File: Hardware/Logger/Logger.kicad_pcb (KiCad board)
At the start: 2 copper layers, 70 x 71 mm, 78 parts, among them CN1 Conn_02x19_Odd_Even, CN10 Conn_02x19_Odd_Even, CN2 Conn_02x19_Odd_Even, CN7 Conn_02x19_Odd_Even, J1 Conn_Coaxial, J10 Conn_01x08_Female, J2 Conn_Coaxial, J3 Conn_Coaxial, J4 Conn_Coaxial, J5 USB_B_Micro, J6 112K-TAA0-RA1_ATTEND, J7 DB9_Female_MountingHoles, J8 Conn_01x06_Female, J9 Conn_01x08_Female, Q5 BC848, Q6 BC848, Q7 BC848, Q8 BC848, SW1 SW_Push, SW2 SW_Push, SW3 SW_Push, SW4 SW_Push, U1 ESP-12E, U2 ST7735S, U3 LD1117ASTR

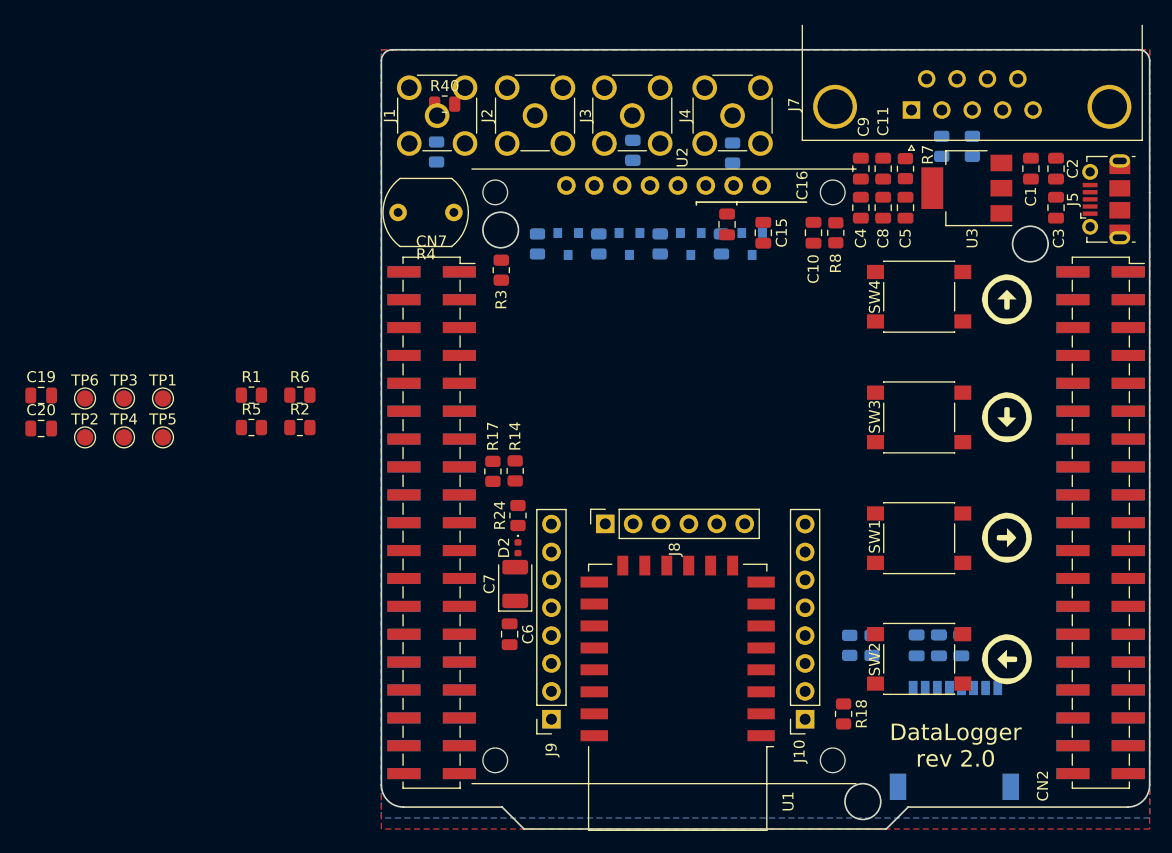
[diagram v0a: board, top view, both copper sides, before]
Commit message: draft of rev 3.0, cleanup of repo from not fully open source libs
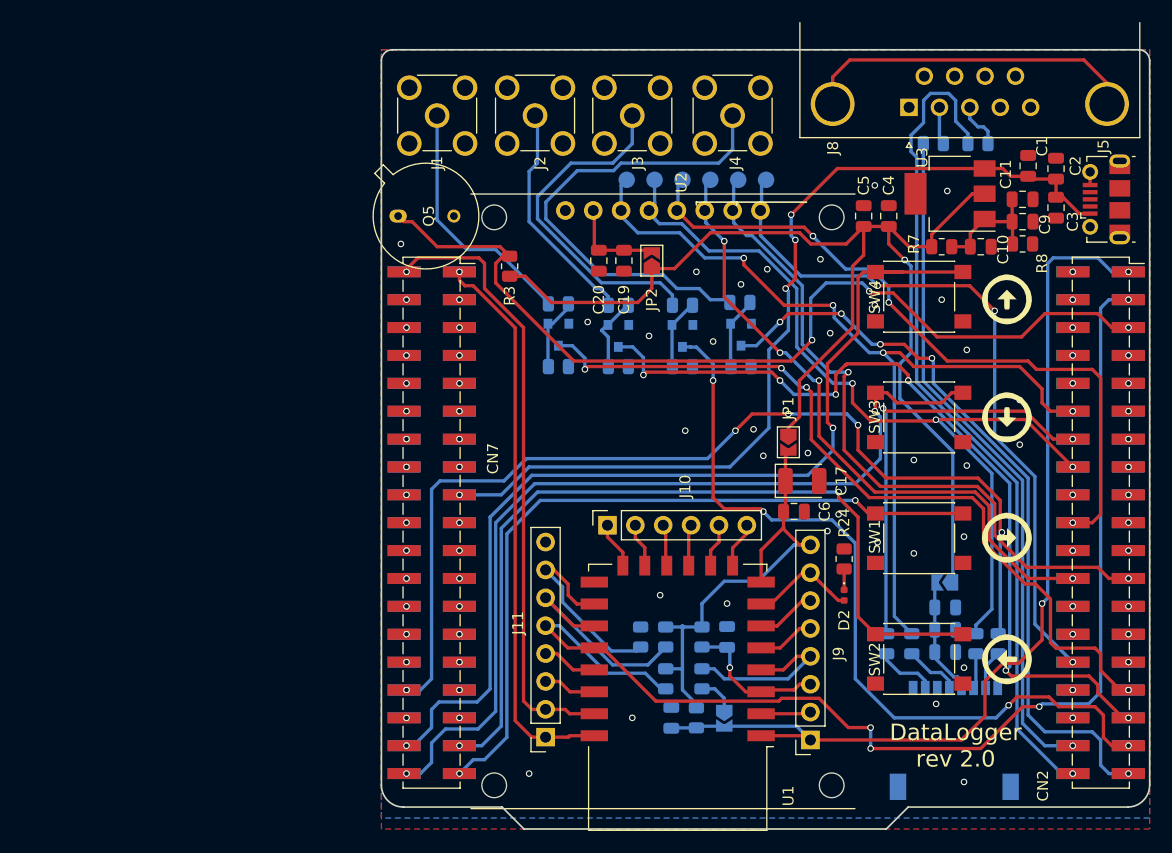
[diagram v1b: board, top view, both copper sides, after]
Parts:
- removed C7: 47u/6V3, Capacitor_Tantalum_SMD:CP_EIA-3528-21_Kemet-B
- removed C8: 330n, Capacitor_SMD:C_0805_2012Metric
- removed J7: DB9_Female_MountingHoles, Connector_Dsub:DSUB-9_Female_Horizontal_P2.77x2.84mm_EdgePinOffset4.94mm_Housed_MountingHolesOffset7.48mm
- removed R4: R_PHOTO, OptoDevice:R_LDR_7x6mm_P5.1mm_Vertical
- added C17: 47u/6V3, Capacitor_Tantalum_SMD:CP_EIA-3528-21_Kemet-B, F.Cu at (168.4, 90.3)
- added J11: Conn_01x08_Socket, Connector_PinSocket_2.54mm:PinSocket_1x08_P2.54mm_Vertical, F.Cu at (145.0, 113.6)
- added JP1: Jumper_2_Small_Open, Jumper:SolderJumper-2_P1.3mm_Open_TrianglePad1.0x1.5mm, F.Cu at (167.1, 86.8)
- added JP2: Jumper_2_Small_Open, Jumper:SolderJumper-2_P1.3mm_Open_TrianglePad1.0x1.5mm, F.Cu at (154.6, 70.2)
- added JP4: Jumper_2_Small_Open, Jumper:SolderJumper-2_P1.3mm_Open_TrianglePad1.0x1.5mm, B.Cu at (181.3, 99.5)
- added JP5: Jumper_2_Small_Open, Jumper:SolderJumper-2_P1.3mm_Open_TrianglePad1.0x1.5mm, B.Cu at (161.2, 111.9)
- added Q5: Q_Photo_NPN, Package_TO_SOT_THT:TO-5-2, F.Cu at (131.5, 66.2)
- added R15: 470R, Resistor_SMD:R_0805_2012Metric, B.Cu at (159.2, 108.3)
- C15, C16, R1, R14, R17, R18, R2, R40, R5, R6, TP1, TP2, TP3, TP4, TP5, TP6: moved to B.Cu
- J10: value Conn_01x08_Female -> Conn_01x06_Socket; footprint Connector_PinSocket_2.54mm:PinSocket_1x08_P2.54mm_Vertical -> Connector_PinSocket_2.54mm:PinSocket_1x06_P2.54mm_Vertical
- J8: value Conn_01x06_Female -> DE9_Plug_MountingHoles; footprint Connector_PinSocket_2.54mm:PinSocket_1x06_P2.54mm_Vertical -> Connector_Dsub:DSUB-9_Female_Horizontal_P2.77x2.84mm_EdgePinOffset4.94mm_Housed_MountingHolesOffset7.48mm
- J9: value Conn_01x08_Female -> Conn_01x08_Socket
- R3: value 1k -> 2M
- moved R1 71.7 mm to (186.2, 105.1), turned to -90 degrees
- moved TP2 66.3 mm to (165.1, 62.9), turned to 180 degrees
- moved R2 64.7 mm to (184.2, 105.1), turned to -90 degrees
- moved R5 63.3 mm to (178.3, 105.1), turned to -90 degrees
- moved TP3 59.4 mm to (162.5, 62.9), turned to 180 degrees
- moved TP4 58.4 mm to (160.0, 62.9), turned to 180 degrees
- moved R6 58.1 mm to (176.0, 105.1), turned to -90 degrees
- moved TP6 55.6 mm to (154.9, 62.9), turned to 180 degrees
- moved C19 54.5 mm to (152.1, 70.2), turned to -90 degrees
- moved C20 53.1 mm to (149.8, 70.2), turned to -90 degrees
- moved TP5 52.8 mm to (157.4, 62.9), turned to 180 degrees
- moved J8 47.0 mm to (178.1, 56.2), turned to 180 degrees
- moved TP1 46.7 mm to (152.4, 62.9), turned to 180 degrees
- moved C16 45.2 mm to (156.4, 111.9), turned to 90 degrees
- moved C15 37.0 mm to (161.5, 104.5), turned to 90 degrees
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- renumbered Q5 to Q1, Q6 to Q2, Q7 to Q3, Q8 to Q4
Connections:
- net CS_ESP renamed Net-(CN10-Pin_18)
- net ESP_ENABLE renamed Net-(CN10-Pin_22)
- net MISO renamed SPI1_MISO
- net MOSI renamed SPI1_MOSI
- C12 pad 1: 3V3 -> Net-(J6-VDD)
- C13 pad 1: 3V3 -> Net-(J6-VDD)
- C14 pad 1: 3V3 -> Net-(J6-VDD)
- C19 pad 1: 3V3 -> Net-(JP2-B)
- C20 pad 1: 3V3 -> Net-(JP2-B)
- C6 pad 1: 3V3 -> ESP_PWR
- CN1 pad 1: Net-(CN1-Pad1) -> ESP32_RX
- CN1 pad 2: Net-(CN1-Pad2) -> ESP32_TX
- CN1 pad 31: Net-(CN1-Pad31) -> CS_SD
- CN1 pad 35: Net-(CN1-Pad35) -> KEY_RIGHT
- CN1 pad 36: Net-(CN1-Pad36) -> KEY_UP
- CN1 pad 37: Net-(CN1-Pad37) -> KEY_LEFT
- CN1 pad 38: Net-(CN1-Pad38) -> KEY_DOWN
- CN10 pad 10: CS_LCD -> Net-(CN10-Pin_10)
- CN10 pad 11: Net-(CN10-Pad11) -> SPI1_SCK
- CN10 pad 12: DC_LCD -> Net-(CN10-Pin_12)
- CN10 pad 14: ESP32_TX -> Net-(CN10-Pin_14)
- CN10 pad 16: ESP32_RX -> Net-(CN10-Pin_16)
- CN10 pad 19: Net-(CN10-Pad19) -> SPI1_RST_LCD
- CN10 pad 2: Net-(CN10-Pad2) -> ESP32_RST
- CN10 pad 20: ESP32_FLASH_MODE -> Net-(CN10-Pin_20)
- CN10 pad 23: Net-(CN10-Pad23) -> SPI1_DC_LCD
- CN10 pad 24: KEY_RIGHT -> SPI1_CS_LCD
- CN10 pad 26: KEY_LEFT -> Net-(CN10-Pin_26)
- CN10 pad 28: KEY_DOWN -> Net-(CN10-Pin_28)
- CN10 pad 29: Net-(CN10-Pad29) -> LCD_BRIGHT_PWM
- CN10 pad 30: KEY_UP -> Net-(CN10-Pin_30)
- CN10 pad 31: SCK -> Net-(CN10-Pin_31)
- CN10 pad 35: Net-(CN10-Pad35) -> EXT_RX
- CN10 pad 37: Net-(CN10-Pad37) -> EXT_TX
- CN10 pad 4: Net-(CN10-Pad4) -> ESP32_FLASH_MODE
- CN10 pad 6: EXT_TX -> BACKGROUND_LIGHT_SENSOR
- CN10 pad 8: EXT_RX -> Net-(CN10-Pin_8)
- CN2 pad 1: Net-(CN10-Pad2) -> ESP32_RST
- CN2 pad 11: DC_LCD -> Net-(CN10-Pin_12)
- CN2 pad 12: Net-(CN10-Pad11) -> SPI1_SCK
- CN2 pad 13: ESP32_TX -> Net-(CN10-Pin_14)
- CN2 pad 15: ESP32_RX -> Net-(CN10-Pin_16)
- CN2 pad 19: ESP32_FLASH_MODE -> Net-(CN10-Pin_20)
- CN2 pad 20: Net-(CN10-Pad19) -> SPI1_RST_LCD
- CN2 pad 23: KEY_RIGHT -> SPI1_CS_LCD
- CN2 pad 24: Net-(CN10-Pad23) -> SPI1_DC_LCD
- CN2 pad 25: KEY_LEFT -> Net-(CN10-Pin_26)
- CN2 pad 27: KEY_DOWN -> Net-(CN10-Pin_28)
- CN2 pad 29: KEY_UP -> Net-(CN10-Pin_30)
- CN2 pad 3: Net-(CN10-Pad4) -> ESP32_FLASH_MODE
- CN2 pad 30: Net-(CN10-Pad29) -> LCD_BRIGHT_PWM
- CN2 pad 32: SCK -> Net-(CN10-Pin_31)
- CN2 pad 36: Net-(CN10-Pad35) -> EXT_RX
- CN2 pad 38: Net-(CN10-Pad37) -> EXT_TX
- CN2 pad 5: EXT_TX -> BACKGROUND_LIGHT_SENSOR
- CN2 pad 7: EXT_RX -> Net-(CN10-Pin_8)
- CN2 pad 9: CS_LCD -> Net-(CN10-Pin_10)
- CN7 pad 1: Net-(CN1-Pad2) -> ESP32_TX
- CN7 pad 2: Net-(CN1-Pad1) -> ESP32_RX
- CN7 pad 32: Net-(CN1-Pad31) -> CS_SD
- CN7 pad 35: Net-(CN1-Pad36) -> KEY_UP
- CN7 pad 36: Net-(CN1-Pad35) -> KEY_RIGHT
- CN7 pad 37: Net-(CN1-Pad38) -> KEY_DOWN
- CN7 pad 38: Net-(CN1-Pad37) -> KEY_LEFT
- J10 pad 1: ESP32_RST -> /WiFiInterface/ESP32_SCLK
- J10 pad 2: /WiFiInterface/ESP_ADC -> /WiFiInterface/ESP32_MOSI
- J10 pad 3: /WiFiInterface/EN -> /WiFiInterface/GPIO10
- J10 pad 4: /WiFiInterface/GPIO16 -> /WiFiInterface/GPIO9
- J10 pad 5: /WiFiInterface/GPIO14 -> /WiFiInterface/ESP32_MISO
- J10 pad 6: /WiFiInterface/GPIO12 -> /WiFiInterface/ESP32_CS0
- J5 pad 2: (no net) -> unconnected-(J5-D--Pad2)
- J5 pad 3: (no net) -> unconnected-(J5-D+-Pad3)
- J5 pad 4: (no net) -> unconnected-(J5-ID-Pad4)
- J6 pad 1: (no net) -> unconnected-(J6-NC-Pad1)
- J6 pad 4: 3V3 -> Net-(J6-VDD)
- J6 pad 8: (no net) -> unconnected-(J6-NC-Pad8)
- J8 pad 1: /WiFiInterface/ESP32_SCLK -> unconnected-(J8-Pad1)
- J8 pad 2: /WiFiInterface/ESP32_MOSI -> Net-(J8-Pad2)
- J8 pad 3: /WiFiInterface/GPIO10 -> Net-(J8-Pad3)
- J8 pad 4: /WiFiInterface/GPIO9 -> unconnected-(J8-Pad4)
- J8 pad 5: /WiFiInterface/ESP32_MISO -> unconnected-(J8-Pad5)
- J8 pad 6: /WiFiInterface/ESP32_CS0 -> unconnected-(J8-Pad6)
- J9 pad 1: ESP32_TX -> ESP32_RST
- J9 pad 2: ESP32_RX -> /WiFiInterface/ESP_ADC
- J9 pad 3: /WiFiInterface/GPIO5 -> /WiFiInterface/EN
- J9 pad 4: /WiFiInterface/GPIO4 -> /WiFiInterface/GPIO16
- J9 pad 5: ESP32_FLASH_MODE -> /WiFiInterface/GPIO14
- J9 pad 6: /WiFiInterface/GPIO2 -> /WiFiInterface/GPIO12
- J9 pad 7: /WiFiInterface/GPIO15 -> /WiFiInterface/GPIO13
- J9 pad 8: GND -> ESP_PWR
- R1 pad 1: (no net) -> CS_SD
- R13 pad 1: 3V3 -> ESP_PWR
- R14 pad 1: 3V3 -> ESP_PWR
- R17 pad 1: 3V3 -> ESP_PWR
- R18 pad 1: 3V3 -> ESP_PWR
- R3 pad 2: LIGHT_PROBE -> BACKGROUND_LIGHT_SENSOR
- R36 pad 2: Net-(J7-Pad2) -> Net-(J8-Pad2)
- R37 pad 2: Net-(J7-Pad3) -> Net-(J8-Pad3)
- R5 pad 1: SCK -> SPI1_SCK
- TP1 pad 1: SCK -> SPI1_SCK
- TP3 pad 1: CS_LCD -> SPI1_CS_LCD
- TP4 pad 1: DC_LCD -> SPI1_DC_LCD
- TP5 pad 1: RST_LCD -> SPI1_RST_LCD
- U1 pad 8: 3V3 -> ESP_PWR
- U2 pad 2: 3V3 -> Net-(JP2-B)
- U2 pad 3: SCK -> SPI1_SCK
- U2 pad 5: RST_LCD -> SPI1_RST_LCD
- U2 pad 6: DC_LCD -> SPI1_DC_LCD
- U2 pad 7: CS_LCD -> SPI1_CS_LCD
- U3 pad 4: (no net) -> unconnected-(U3-NC-Pad4)
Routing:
- net 3V3: track 0.00 -> 109.9 mm, vias 0 -> 1
- net ESP32_FLASH_MODE: track 0.00 -> 109.0 mm, vias 0 -> 4
- net CS_SD: track 0.00 -> 91.5 mm, vias 0 -> 5
- net KEY_RIGHT: track 0.00 -> 88.9 mm, vias 0 -> 2
- net ESP32_RST: track 0.00 -> 86.4 mm, vias 0 -> 2
- net BACKGROUND_LIGHT_SENSOR: track 0.00 -> 84.5 mm, vias 0 -> 3
- net 5V: track 0.00 -> 82.8 mm, vias 0 -> 4
- net KEY_LEFT: track 0.00 -> 81.1 mm, vias 0 -> 2
- net SPI1_SCK: track 0.00 -> 79.9 mm, vias 0 -> 4
- net SPI1_MOSI: track 0.00 -> 78.6 mm, vias 0 -> 3
- net KEY_UP: track 0.00 -> 77.0 mm, vias 0 -> 2
- net ANALOG_IN_2: track 0.00 -> 75.8 mm, vias 0 -> 6
- net EXT_TX: track 0.00 -> 75.3 mm, vias 0 -> 1
- net ANALOG_IN_3: track 0.00 -> 72.8 mm, vias 0 -> 4
- net ANALOG_IN_1: track 0.00 -> 72.5 mm, vias 0 -> 4
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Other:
- outline, holes or cut-outs redrawn

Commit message: cmake cleanup
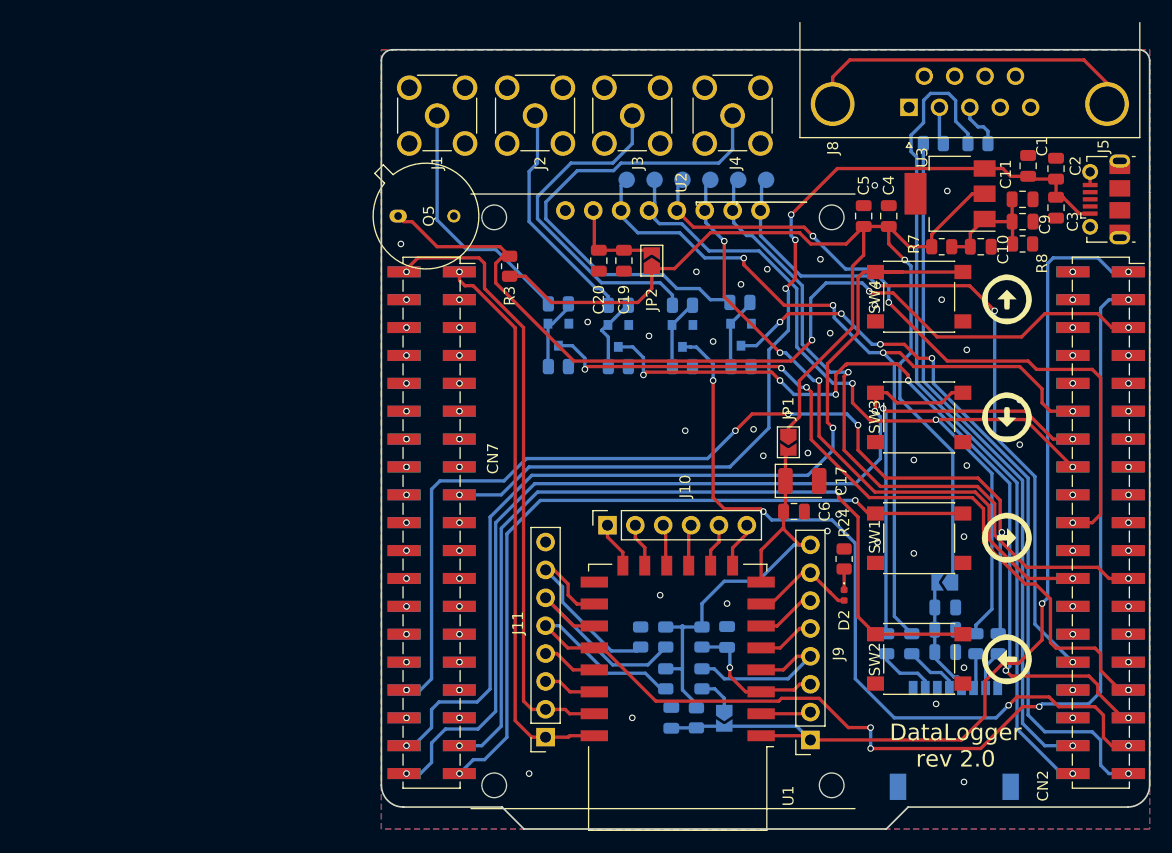
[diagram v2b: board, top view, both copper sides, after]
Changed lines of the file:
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@@
 		(net 3)
 		(net_name "GND")
-		(layer "F.Cu")
+		(layers "F&B.Cu")
 		(hatch edge 0.508)
 		(connect_pads
@@
 		(min_thickness 0.254)
 		(filled_areas_thickness no)
-		(fill yes
+		(fill
 			(thermal_gap 0.508)
 			(thermal_bridge_width 0.508)
@@
 			)
 		)
-	)
-	(zone
-		(net 3)
-		(net_name "GND")
-		(layer "B.Cu")
-		(hatch edge 0.508)
-		(connect_pads
-			(clearance 0.508)
-		)
-		(min_thickness 0.254)
-		(filled_areas_thickness no)
-		(fill yes
-			(thermal_gap 0.508)
-			(thermal_bridge_width 0.508)
-		)
-		(polygon
-			(pts
-				(xy 200 121) (xy 130 121) (xy 130 51) (xy 200 51)
-			)
-		)
